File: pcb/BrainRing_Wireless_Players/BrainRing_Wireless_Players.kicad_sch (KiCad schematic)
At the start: 14 parts, among them J1 LED_Strip, J2 Arcade_Button, J3 Jumper, J4 Jumper, Q1 MMBT2222A, U1 LGT8F328P_LQFP32, U2 NRF24L01_Breakout, U3 MLT-8530

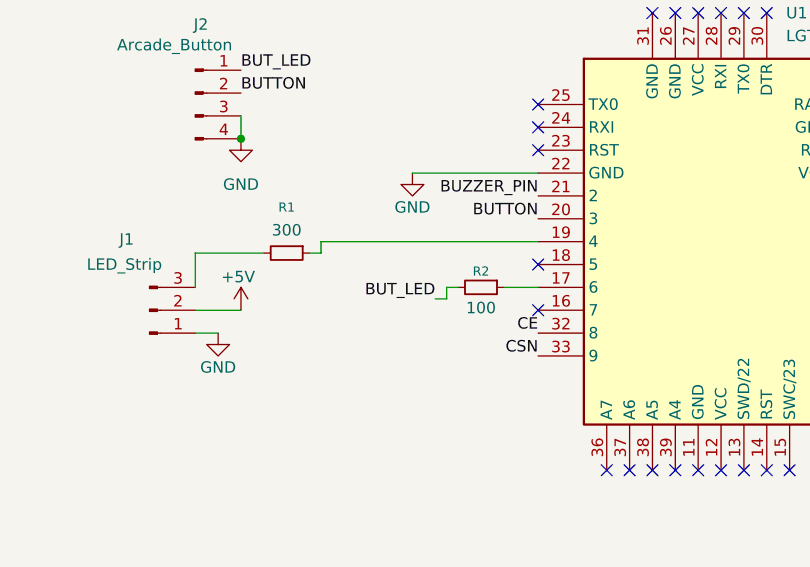
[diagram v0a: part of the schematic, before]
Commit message: Refactor firmware: fair first-press detection, single player firmware, animations
- Shared protocol/radio config (include/brainring.h) and non-blocking melody player (include/melody.h)
- Admin: timestamp-based winner resolution with 30 ms decision window, reject pre-reset presses,
  fresh ACK payloads, press/reset sound and LED indication, idle breathing
- Players: one firmware for all boards, ID/color stored in EEPROM with on-device color menu,
  reliable press delivery with per-ID retry delays, link-loss detection,
  strip + button LED (PWM) animations, 3 random win melodies and a lose melody
- Admin case generator, print files and PCB updates

Co-Authored-By: Claude Opus 5.5 <noreply@anthropic.com>
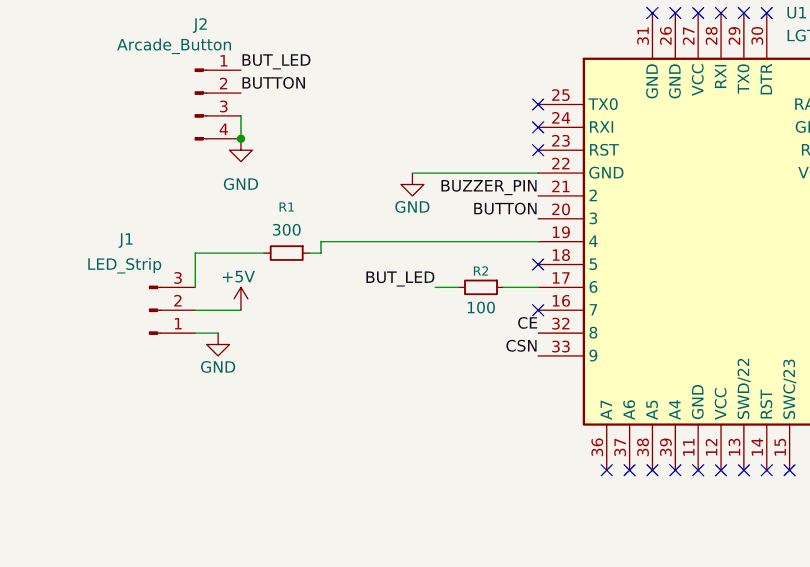
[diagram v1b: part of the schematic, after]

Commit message: Players board Rev. 2.1: IP5305 keep-alive load
- Schematic/PCB: AO3400A (Q2) + 47 Ohm load (R10), gate R8 100 / R9 100k,
  driven from U1 A3 — same circuit as the Admin board. Placed on B.Cu
  under the MCU module; main parts and case-related positions unchanged.
- GND via enlarged to 1.6/0.8 mm for a top-side wire jumper to U1 GND.
- Player firmware: 300 ms pulse every 15 s on A3 so IP5305 doesn't shut
  the 5V output down at light load.
- Regenerated laser-printer sheets (B.Cu, mirrored F.Silkscreen).

Co-Authored-By: Claude Opus 5.5 <noreply@anthropic.com>
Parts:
- added Q2: AO3400A, Package_TO_SOT_SMD:SOT-23, symbol Transistor_FET:AO3400A
- added R10: 47, Resistor_SMD:R_1206_3216Metric, symbol Device:R_Small
- added R8: 100, Resistor_SMD:R_0603_1608Metric, symbol Device:R_Small
- added R9: 100k, Resistor_SMD:R_0603_1608Metric, symbol Device:R_Small
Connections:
- net +5V: now also R10.1
- net GND: now also Q2.2 (S), R9.2
- net KEEPALIVE: now reaches U1.5 (A3)
- net KEEPALIVE: now also R8.1
- new net: Q2.1 (G), R8.2, R9.1
- new net: Q2.3 (D), R10.2
- no-connect marks 28 -> 27
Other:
- note added: "~100 mA / 300 ms every 15 s on +5V, so IP5305 does not cut the light load"
